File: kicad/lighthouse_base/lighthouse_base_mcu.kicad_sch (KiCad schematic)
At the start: 2 parts, among them U1 STM32L412R8Tx, U2 RV-3028-C7

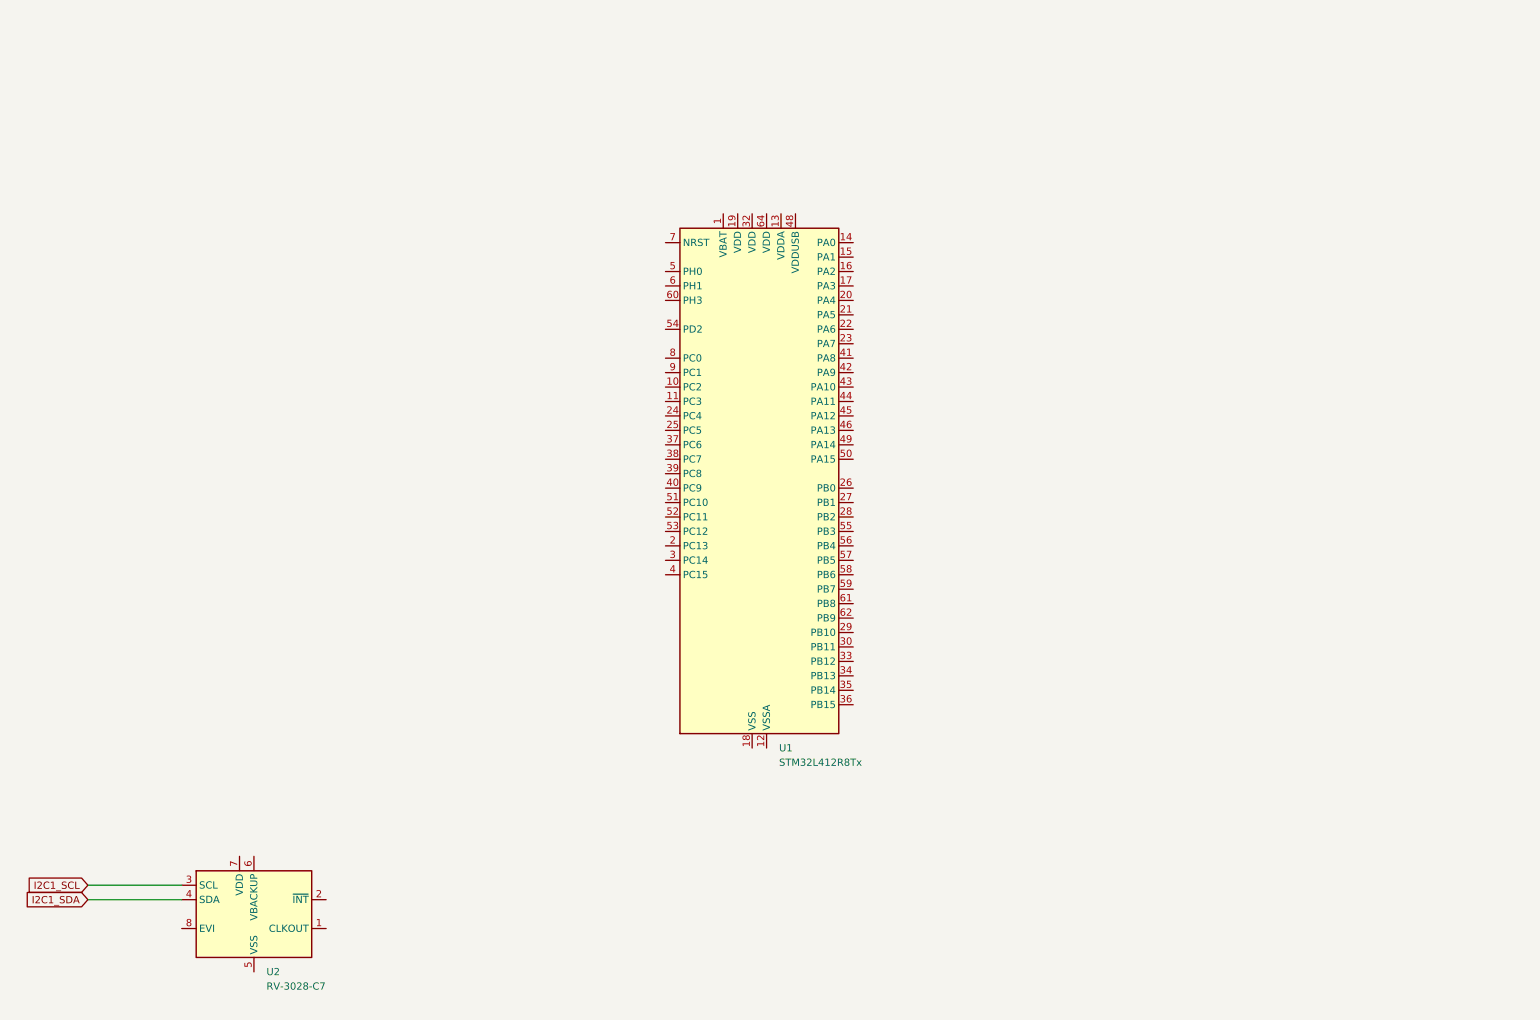
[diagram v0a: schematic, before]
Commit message: added FPPlayer and BC805M BLE Module
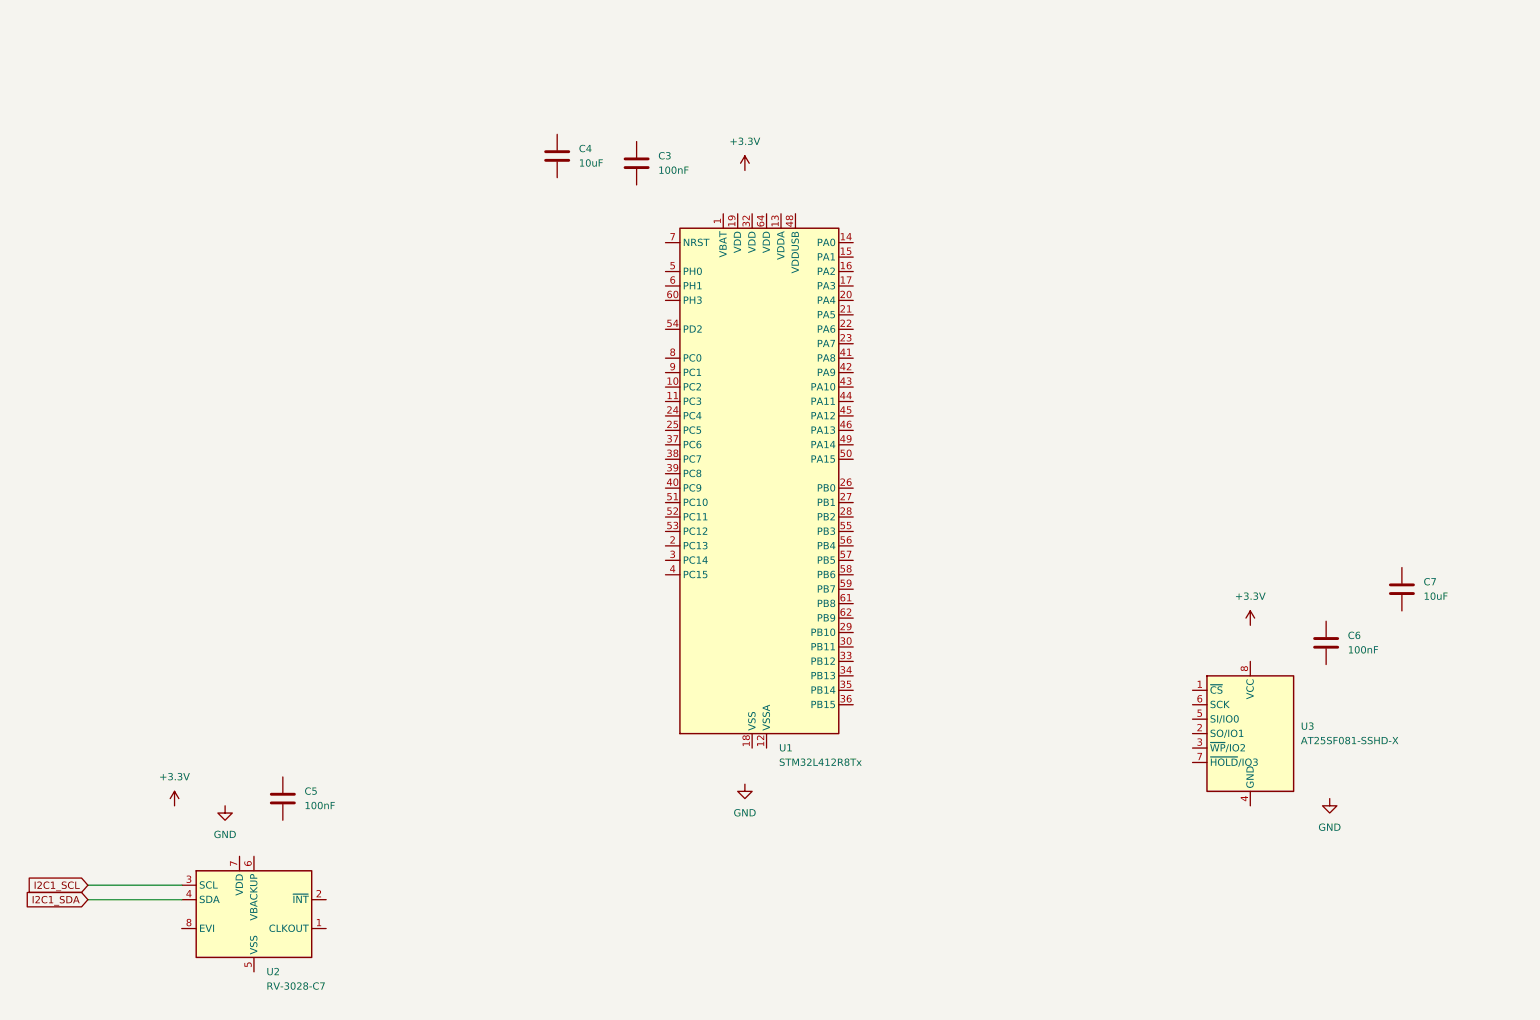
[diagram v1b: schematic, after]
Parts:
- added C3, C5, C6: 100nF, symbol Device:C
- added C4, C7: 10uF, symbol Device:C
- added U3: AT25SF081-SSHD-X, Package_SO:SOIC-8_3.9x4.9mm_P1.27mm, symbol Memory_Flash:AT25SF081-SSHD-X

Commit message: schema v1 done
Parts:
- added BT1: Keystone 3002, Battery:BatteryHolder_Keystone_3002_1x2032, symbol Device:Battery_Cell
- added C10, C8, C9: 100nF, symbol Device:C
- added J9: Conn_01x07, symbol Connector_Generic:Conn_01x07
- added R3, R4, R5, R6: 0R, symbol Device:R
- added SW1: ~, Lighthouse1:PTS526, symbol lighthouse1:SW_PTS5236
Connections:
- net +3.3V: now also C3.1, C4.1, C5.1, C6.1, C7.1, U1.1 (VBAT), U1.13 (VDDA), U1.19 (VDD), U1.32 (VDD), U1.48 (VDDUSB), U1.64 (VDD), U2.7 (VDD), U3.3 (~{WP}/IO2), U3.7 (~{HOLD}/IO3), U3.8 (VCC), C10.1, C8.1, C9.1, J9.1 (Pin_1)
- net GND: now also C3.2, C4.2, C5.2, C6.2, C7.2, U1.12 (VSSA), U1.18 (VSS), U1.31 (VSS), U1.47 (VSS), U1.63 (VSS), U2.5 (VSS), U3.4 (GND), BT1.2 (-), C10.2, C8.2, C9.2, J9.2 (Pin_2), SW1.3, SW1.4
- net I2C1_SCL: now also U1.42 (PA9)
- net I2C1_SDA: now also U1.43 (PA10)
- net RTC_CLK: now reaches U2.1 (CLKOUT)
- net RTC_CLK: now also U1.8 (PC0)
- net ~{RTC_INT}: now reaches U2.2 (~{INT})
- net ~{RTC_INT}: now also U1.39 (PC8)
- net at U2.6 (VBACKUP): now also BT1.1 (+)
- net WHITE_PWM1: now reaches U1.14 (PA0)
- net WHITE_PWM2: now reaches U1.15 (PA1)
- net at U1.16 (PA2): now also R3.1
- net at U1.17 (PA3): now also R4.1
- net ~{SPI1_CS}: now reaches U1.20 (PA4)
- net ~{SPI1_CS}: now also U3.1 (~{CS})
- net SPI_SCLK: now reaches U1.21 (PA5)
- net SPI_SCLK: now also U3.6 (SCK)
- net SPI1_CIPO: now reaches U1.22 (PA6)
- net SPI1_CIPO: now also U3.2 (SO/IO1)
- net SPI1_COPI: now reaches U1.23 (PA7)
- net SPI1_COPI: now also U3.5 (SI/IO0)
- net at U1.24 (PC4): now also R5.2
- net at U1.25 (PC5): now also R6.2
- net BTN0: now reaches U1.26 (PB0)
- net BTN1: now reaches U1.27 (PB1)
- net BTN2: now reaches U1.28 (PB2)
- net ~{IS_SDB}: now reaches U1.37 (PC6)
- net ~{IS_INTB}: now reaches U1.38 (PC7)
- net USB_D-: now reaches U1.44 (PA11)
- net USB_D+: now reaches U1.45 (PA12)
- net STM_SWDIO: now reaches U1.46 (PA13)
- net STM_SWDIO: now also J9.3 (Pin_3)
- net STM_SWDCLK: now reaches U1.49 (PA14)
- net STM_SWDCLK: now also J9.4 (Pin_4)
- net BTN3: now reaches U1.55 (PB3)
- net BTN4: now reaches U1.56 (PB4)
- net DBG_TX: now reaches U1.58 (PB6)
- net DBG_TX: now also J9.6 (Pin_6)
- net DBG_RX: now reaches U1.59 (PB7)
- net DBG_RX: now also J9.7 (Pin_7)
- net ~{STM_RST}: now reaches U1.7 (NRST)
- net ~{STM_RST}: now also J9.5 (Pin_5), SW1.1, SW1.2
- new net BLE_RX: R6.1
- new net BLE_TX: R5.1
- new net SOUND_RX: R4.2
- new net SOUND_TX: R3.2
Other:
- moved on the sheet: C3, C4, C5, C6, C7, U1, U3

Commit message: schematics done
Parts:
- added R11, R12: 1M, Resistor_SMD:R_0603_1608Metric_Pad0.98x0.95mm_HandSolder, symbol Device:R
- added TP1, TP10, TP11, TP12, TP13, TP14, TP15, TP16, TP17, TP18, TP19, TP2, TP20, TP21, TP22, TP23, TP24, TP3, TP4, TP5, TP7, TP8, TP9: TestPoint, TestPoint:TestPoint_Pad_D1.5mm, symbol Connector:TestPoint
- C10: renamed from C9; footprint (none) -> Capacitor_SMD:C_0201_0603Metric_Pad0.64x0.40mm_HandSolder
- C11: renamed from C10; footprint (none) -> Capacitor_SMD:C_0201_0603Metric_Pad0.64x0.40mm_HandSolder
- C12: renamed from C7; footprint (none) -> Capacitor_SMD:C_0603_1608Metric_Pad1.08x0.95mm_HandSolder
- C13: renamed from C6; footprint (none) -> Capacitor_SMD:C_0201_0603Metric_Pad0.64x0.40mm_HandSolder
- C14: renamed from C5; footprint (none) -> Capacitor_SMD:C_0201_0603Metric_Pad0.64x0.40mm_HandSolder
- C7: renamed from C4; footprint (none) -> Capacitor_SMD:C_0201_0603Metric_Pad0.64x0.40mm_HandSolder
- C8: renamed from C3; footprint (none) -> Capacitor_SMD:C_0201_0603Metric_Pad0.64x0.40mm_HandSolder
- C9: renamed from C8; footprint (none) -> Capacitor_SMD:C_0201_0603Metric_Pad0.64x0.40mm_HandSolder
- J3: renamed from J9; footprint (none) -> Connector_PinHeader_1.27mm:PinHeader_1x07_P1.27mm_Vertical
- R10: renamed from R6; footprint (none) -> Resistor_SMD:R_0603_1608Metric_Pad0.98x0.95mm_HandSolder
- R7: renamed from R3; footprint (none) -> Resistor_SMD:R_0603_1608Metric_Pad0.98x0.95mm_HandSolder
- R8: renamed from R4; footprint (none) -> Resistor_SMD:R_0603_1608Metric_Pad0.98x0.95mm_HandSolder
- R9: renamed from R5; footprint (none) -> Resistor_SMD:R_0603_1608Metric_Pad0.98x0.95mm_HandSolder
- renumbered BT1 to BT2, U1 to U5, U3 to U6, U2 to U7
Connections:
- net GND: now also R12.1
- net at U5.10 (PC2): now also R11.1, R12.2
- net at U5.11 (PC3): now also TP7.1
- net at U5.2 (PC13): now also TP13.1
- net at U5.29 (PB10): now also TP19.1
- net at U5.3 (PC14): now also TP14.1
- net at U5.30 (PB11): now also TP20.1
- net at U5.33 (PB12): now also TP21.1
- net at U5.34 (PB13): now also TP22.1
- net at U5.35 (PB14): now also TP23.1
- net at U5.36 (PB15): now also TP24.1
- net at U5.4 (PC15): now also TP16.1
- net at U5.40 (PC9): now also TP9.1
- net at U5.41 (PA8): now also TP5.1
- net at U5.5 (PH0): now also TP1.1
- net at U5.50 (PA15): now also TP8.1
- net at U5.51 (PC10): now also TP10.1
- net at U5.52 (PC11): now also TP11.1
- net at U5.53 (PC12): now also TP12.1
- net at U5.54 (PD2): now also TP4.1
- net at U5.57 (PB5): now also TP15.1
- net at U5.6 (PH1): now also TP2.1
- net at U5.60 (PH3): now also TP3.1
- net at U5.61 (PB8): now also TP17.1
- net at U5.62 (PB9): now also TP18.1
- net CH_STAT: now reaches U5.9 (PC1)
- new net +BATT: R11.2

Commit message: started with pcb lighthouse_base
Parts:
- added D5: PMEG4002EJ, Diode_SMD:D_SOD-323F, symbol Diode:PMEG4002EJ
- added R13, R14: 4k7, Resistor_SMD:R_0603_1608Metric_Pad0.98x0.95mm_HandSolder, symbol Device:R
- added R15: 10k, Resistor_SMD:R_0603_1608Metric_Pad0.98x0.95mm_HandSolder, symbol Device:R
- C10, C11, C13, C14, C7, C8, C9: footprint Capacitor_SMD:C_0201_0603Metric_Pad0.64x0.40mm_HandSolder -> Capacitor_SMD:C_0603_1608Metric_Pad1.08x0.95mm_HandSolder
- C12: footprint Capacitor_SMD:C_0603_1608Metric_Pad1.08x0.95mm_HandSolder -> Capacitor_SMD:C_0805_2012Metric_Pad1.18x1.45mm_HandSolder
- SW1: footprint Lighthouse1:PTS526 -> lighthouse:PTS526
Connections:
- net +3.3V: now also R13.2, R14.2, R15.2
- net I2C1_SCL: now also R13.1
- net I2C1_SDA: now also R14.1
- net ~{STM_RST}: now also R15.1
- net at U7.6 (VBACKUP): now also D5.1 (K); no longer BT2.1 (+)
- new net: BT2.1 (+), D5.2 (A)
- no-connect marks 0 -> 1

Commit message: lighthouse base rev 1 done
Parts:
- removed TP19, TP20, TP5, TP7, TP8, TP9: TestPoint, TestPoint:TestPoint_Pad_D1.5mm, symbol Connector:TestPoint
- added J10: Conn_01x07, Connector_PinHeader_2.54mm:PinHeader_1x07_P2.54mm_Vertical, symbol Connector_Generic:Conn_01x07
- added J9: Conn_01x04, Connector_PinHeader_2.54mm:PinHeader_1x04_P2.54mm_Vertical, symbol Connector_Generic:Conn_01x04
- C7: footprint Capacitor_SMD:C_0603_1608Metric_Pad1.08x0.95mm_HandSolder -> Capacitor_SMD:C_0805_2012Metric_Pad1.18x1.45mm_HandSolder
- TP1, TP10, TP11, TP12, TP13, TP14, TP15, TP16, TP17, TP18, TP2, TP21, TP22, TP23, TP24, TP3, TP4: footprint TestPoint:TestPoint_Pad_D1.5mm -> TestPoint:TestPoint_Pad_D1.0mm
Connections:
- net +3.3V: now also J10.1 (Pin_1), J9.1 (Pin_1)
- net GND: now also J10.7 (Pin_7), J9.4 (Pin_4)
- net I2C1_SCL: now also J9.2 (Pin_2)
- net I2C1_SDA: now also J9.3 (Pin_3)
- net SPI1_CIPO: now also J10.5 (Pin_5)
- net SPI1_COPI: now also J10.6 (Pin_6)
- net ~{SPI1_CS1}: now reaches U5.41 (PA8)
- net ~{SPI1_CS1}: now also J10.2 (Pin_2)
- net ~{SPI1_CS2}: now reaches U5.50 (PA15)
- net ~{SPI1_CS2}: now also J10.3 (Pin_3)
- net SPI_SCLK renamed SPI1_SCLK
- net SPI1_SCLK: now also J10.4 (Pin_4)

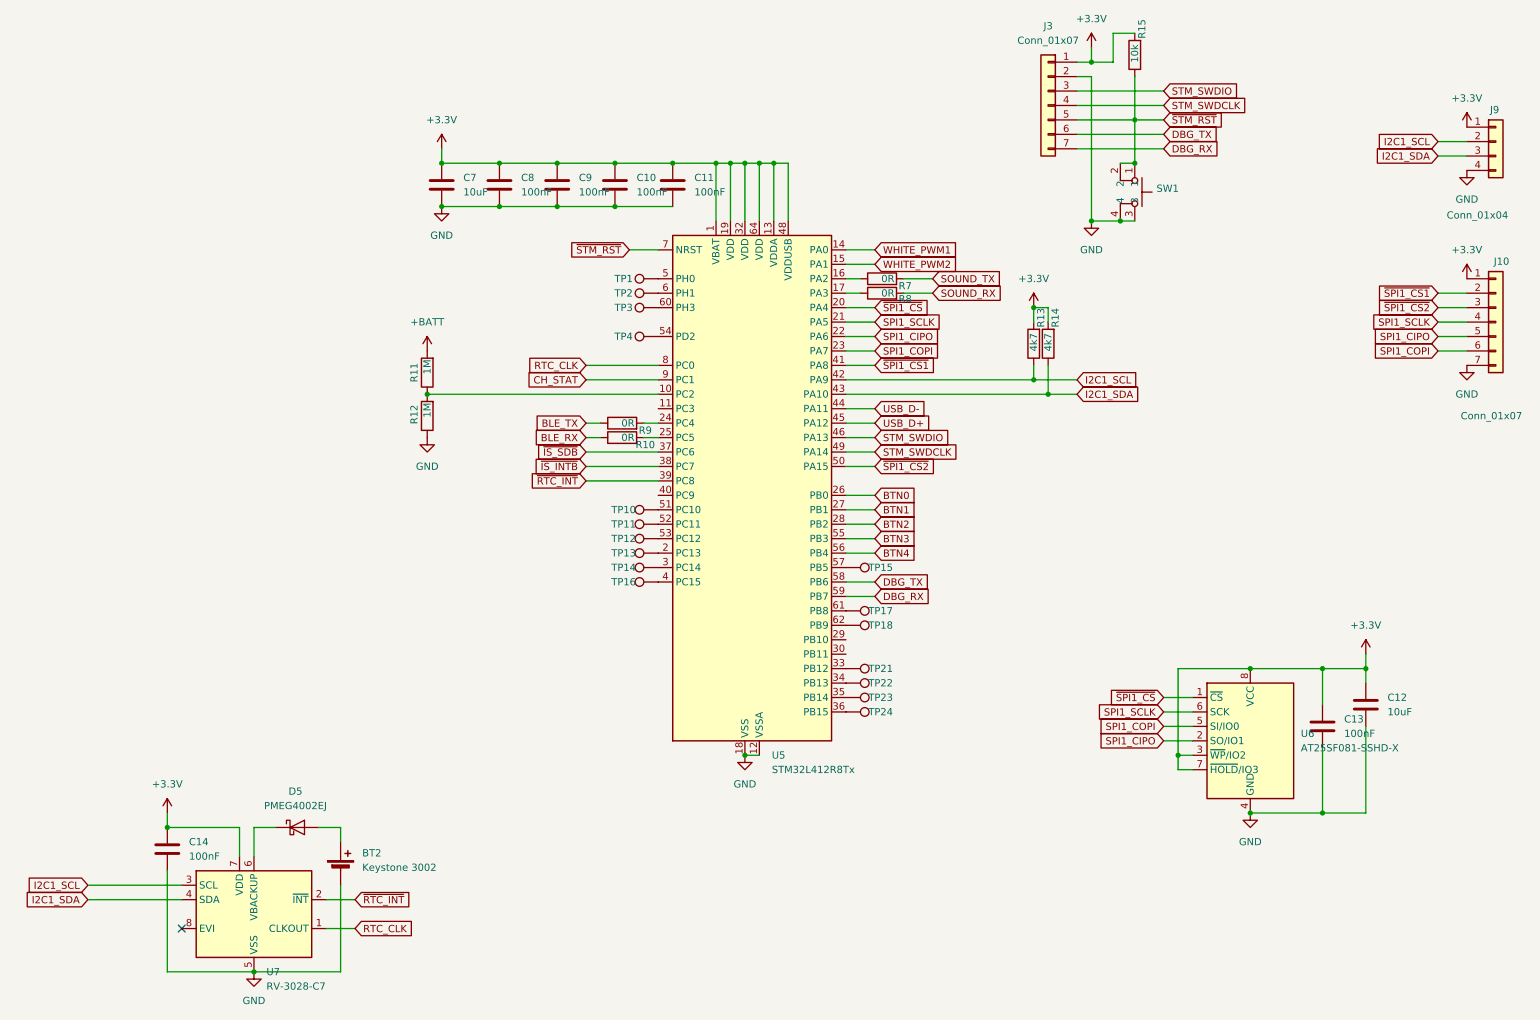
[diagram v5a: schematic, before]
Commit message: rev1: added 32 kHz XTAL, interrupt signals for VBUS + +5V, ... many more
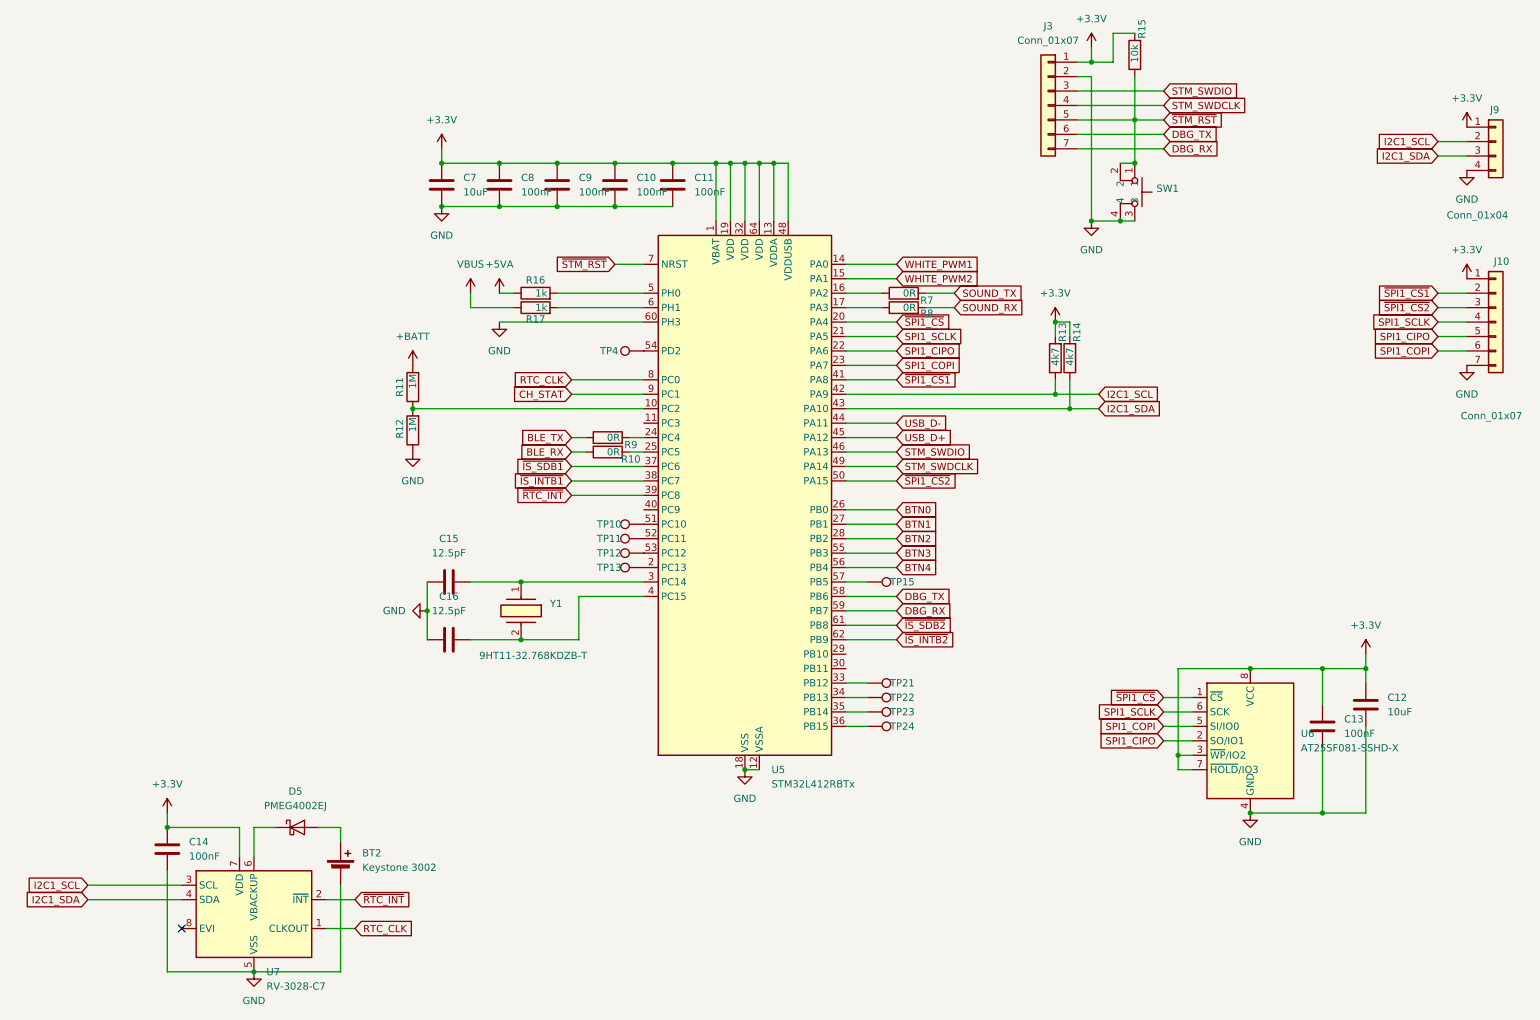
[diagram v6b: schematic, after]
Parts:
- removed TP1, TP14, TP16, TP17, TP18, TP2, TP3: TestPoint, TestPoint:TestPoint_Pad_D1.0mm, symbol Connector:TestPoint
- added C15, C16: 12.5pF, Capacitor_SMD:C_0603_1608Metric_Pad1.08x0.95mm_HandSolder, symbol Device:C
- added R16, R17: 1k, Resistor_SMD:R_0603_1608Metric_Pad0.98x0.95mm_HandSolder, symbol Device:R
- added Y1: 9HT11-32.768KDZB-T, Lighthouse1:9HT1132768KDZBT, symbol lighthouse1:9HT11-32.768KDZB-T
- U5: value STM32L412R8Tx -> STM32L412RBTx; symbol MCU_ST_STM32L4:STM32L412R8Tx -> MCU_ST_STM32L4:STM32L412RBTx
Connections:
- net GND: now also U5.60 (PH3), C15.2, C16.2
- net at U5.5 (PH0): now also R16.2
- net at U5.3 (PC14): now also C15.1, Y1.1
- net ~{IS_SDB2}: now reaches U5.61 (PB8)
- net ~{IS_INTB2}: now reaches U5.62 (PB9)
- net at U5.4 (PC15): now also C16.1, Y1.2
- net at U5.6 (PH1): now also R17.2
- net ~{IS_INTB} renamed ~{IS_INTB1}
- net ~{IS_SDB} renamed ~{IS_SDB1}
- new net +5VA: R16.1
- new net VBUS: R17.1
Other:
- moved on the sheet: R10, R11, R12, R13, R14, R7, R8, R9, TP10, TP11, TP12, TP13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
